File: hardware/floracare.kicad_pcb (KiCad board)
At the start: 2 copper layers, 100 x 100 mm, 17 parts, among them J2 Conn_01x04_Socket, J3 USB_C_Receptacle_USB2.0_16P, J4 Conn_01x04_Socket, J5 Conn_01x14_Socket, J6 Conn_01x05_Socket, U1 AMS1117-3.3, U2 ESP32-S3-WROOM-1

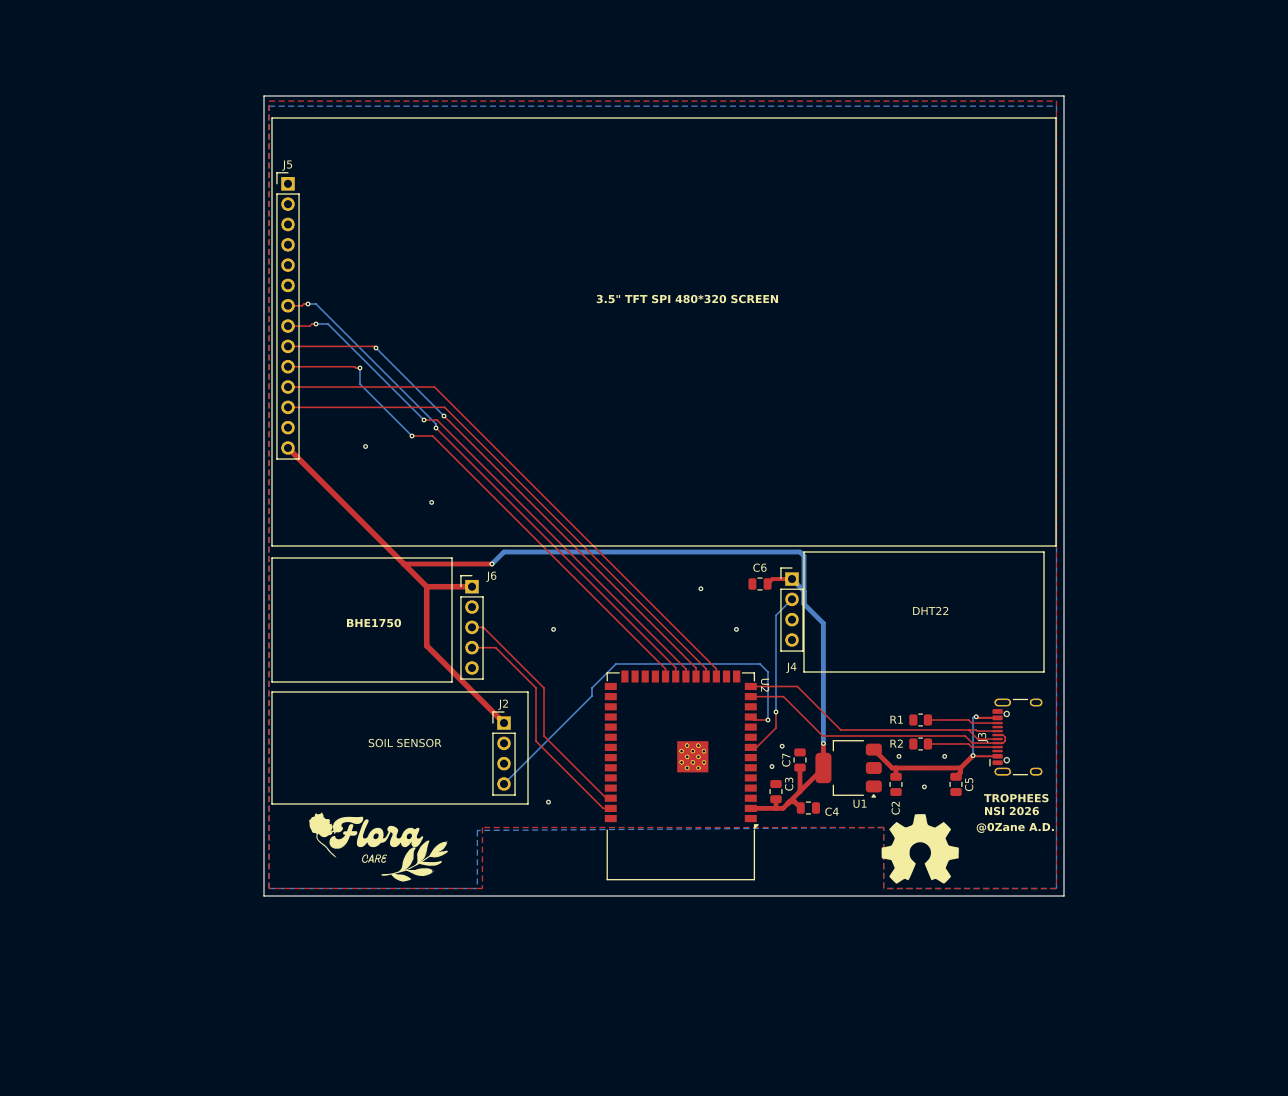
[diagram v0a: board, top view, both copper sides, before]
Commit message: Fixing PCB + adding BOOT and RESET BUTTONS [DRC NOT STABLE]
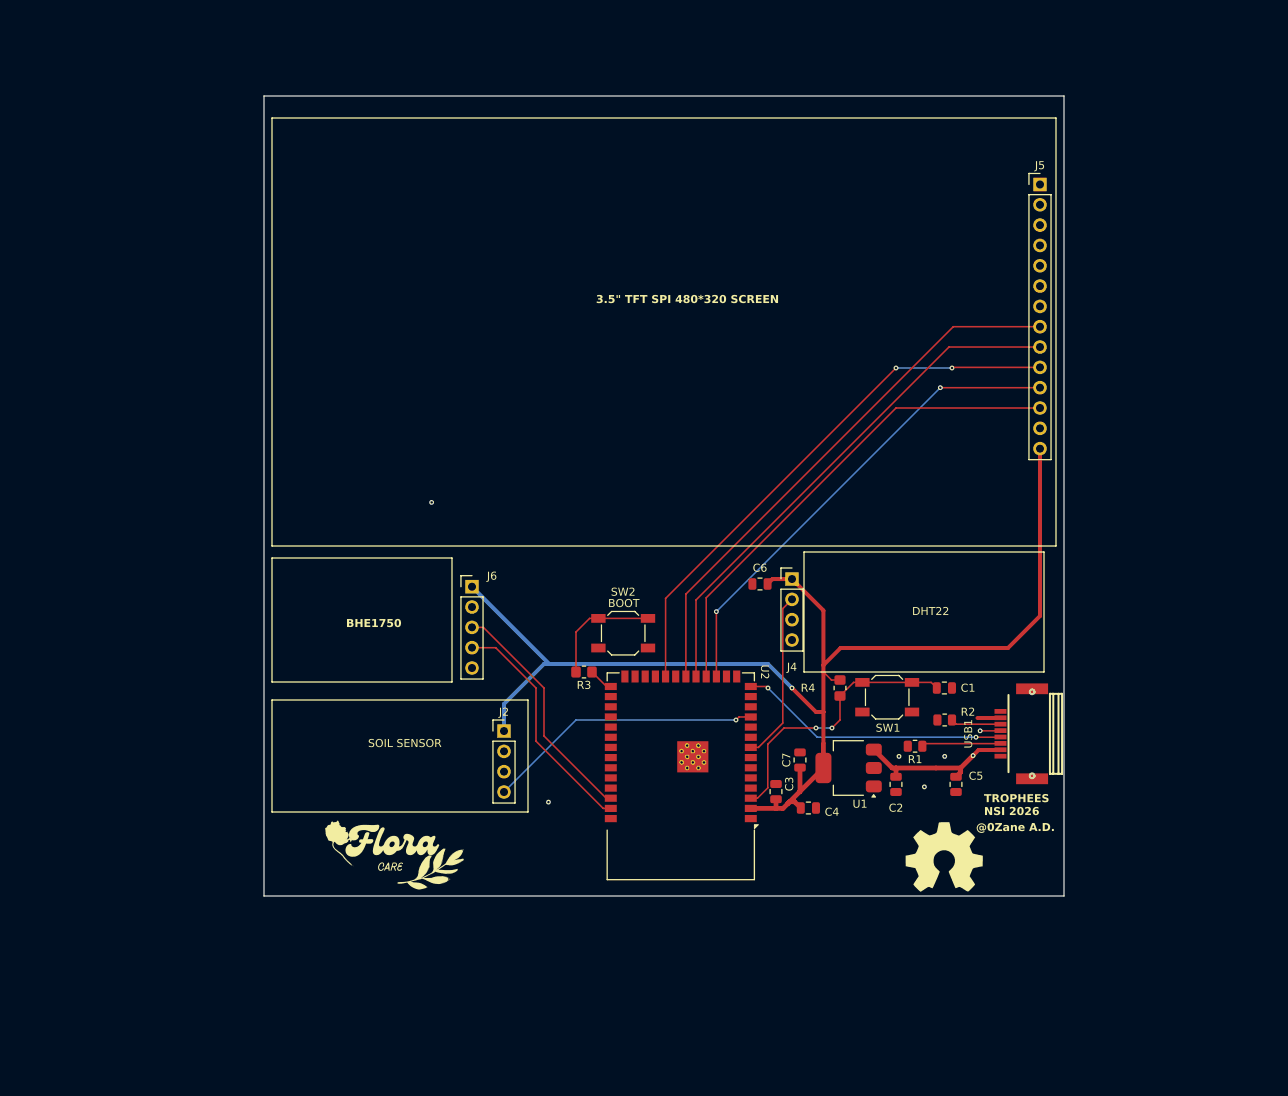
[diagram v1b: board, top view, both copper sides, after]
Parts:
- removed J3: USB_C_Receptacle_USB2.0_16P, Connector_USB:USB_C_Receptacle_HCTL_HC-TYPE-C-16P-01A
- added C1: 0.1uF, Capacitor_SMD:C_0805_2012Metric, F.Cu at (225.5, 99.8)
- added R3: 100, Resistor_SMD:R_0805_2012Metric_Pad1.20x1.40mm_HandSolder, F.Cu at (180.4, 97.8)
- added R4: 5.1K, Resistor_SMD:R_0805_2012Metric_Pad1.20x1.40mm_HandSolder, F.Cu at (212.4, 99.8)
- added SW1: SW_Push, Button_Switch_SMD:SW_SPST_SKQG_WithStem, F.Cu at (218.3, 101.0)
- added SW2: SW_Push, Button_Switch_SMD:SW_SPST_SKQG_WithStem, F.Cu at (185.3, 93.0)
- added USB1: GT-USB-7100A, easyeda2kicad:USB-C-SMD_GT-USB-7100A, F.Cu at (234.5, 105.6)
- moved J5 94.0 mm to (237.4, 36.9)
- moved R2 4.25 mm to (225.5, 103.8)
- moved R1 3.35 mm to (221.8, 107.1)
- moved G*** 3.16 mm to (225.4, 120.8)
- moved G*** 2.24 mm to (156.4, 120.8)
- moved J2 1.00 mm to (170.4, 105.2)
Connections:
- U2 pad 27: unconnected-(U2-IO0-Pad27) -> BOOT
- U2 pad 3: unconnected-(U2-EN-Pad3) -> RESET
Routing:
- net LED: track 68.8 -> 0.00 mm, vias 2 -> 0
- net RESET: track 0.00 -> 34.5 mm, vias 0 -> 2
- net DATA-: track 35.8 -> 2.96 mm, vias 0 -> 1
- net Net-(R3-Pad2): track 0.00 -> 14.7 mm
- net AO_SOIL: track 48.5 -> 35.3 mm
- net RES: track 69.1 -> 60.2 mm, vias 0 -> 2
- net +3V3: track 154.0 -> 160.9 mm, vias 2 -> 1
- net +5V: track 27.4 -> 21.9 mm, vias 2 -> 1
- net CS: track 66.8 -> 61.4 mm
- net DC: track 65.2 -> 68.5 mm
- net BOOT: track 0.00 -> 3.10 mm
- net MOSI: track 68.7 -> 65.7 mm, vias 2 -> 0
- net DATA+: track 37.2 -> 34.3 mm, vias 0 -> 2
- net Net-(USB1-CC2): track 8.87 -> 6.28 mm
- net Net-(USB1-CC1): track 8.87 -> 10.3 mm
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- removed copper zone on B.Cu, net GND
- removed copper zone on F.Cu, net GND
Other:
- board text added: "BOOT"

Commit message: Updating general Project
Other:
- board text added: "RESET"
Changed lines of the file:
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@@
 		(tags "SPST Button Switch")
 		(property "Reference" "SW1"
-			(at 0.1 3.85 0)
+			(at 0.1 -4.15 0)
 			(layer "F.SilkS")
 			(effects
@@
 		)
 		(property "Value" "SW_Push"
-			(at 0.1 -4.15 0)
+			(at 6.1 -4.15 0)
 			(layer "F.Fab")
 			(effects
@@
 		(tags "capacitor")
 		(property "Reference" "C6"
-			(at 0 2 0)
+			(at 0 -2 0)
 			(layer "F.SilkS")
 			(effects
@@
 	)
 	(gr_text "TROPHEES \nNSI 2026\n"
-		(at 230.42 115.85 0)
+		(at 231.42 120.85 0)
 		(layer "F.SilkS")
 		(effects
@@
 	)
 	(gr_text "@0Zane A.D."
-		(at 229.42 117.85 0)
+		(at 230.42 123.85 0)
 		(layer "F.SilkS")
 		(effects
@@
 			)
 			(justify left bottom)
+		)
+	)
+	(gr_text "RESET\n"
+		(at 212.62 105.25 0)
+		(layer "F.SilkS")
+		(effects
+			(font
+				(size 1 1)
+				(thickness 0.1)
+			)
+			(justify left bottom)

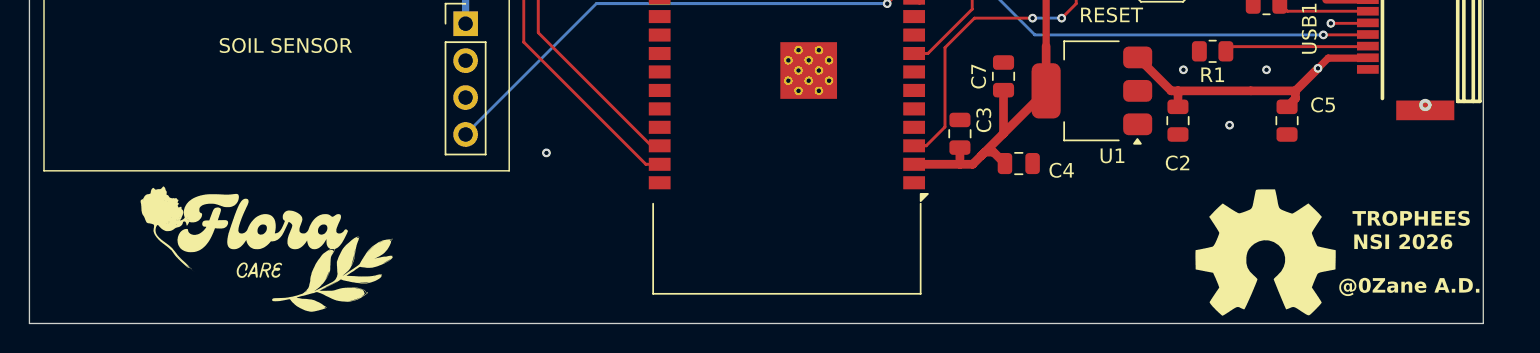
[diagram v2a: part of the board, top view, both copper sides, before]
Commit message: Adding 2 mounting holes
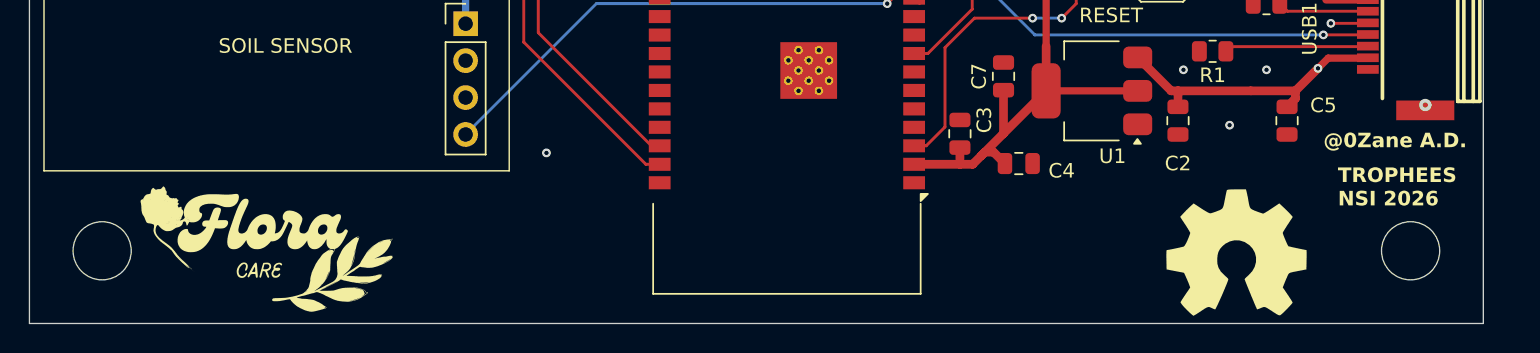
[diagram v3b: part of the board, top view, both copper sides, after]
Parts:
- moved G*** 2.00 mm to (223.4, 120.8)
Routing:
- net +3V3: track 160.9 -> 167.2 mm
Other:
- outline, holes or cut-outs redrawn
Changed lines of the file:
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@@
 	(footprint "LOGO"
 		(layer "F.Cu")
-		(at 225.42 120.85)
+		(at 223.42 120.85)
 		(property "Reference" "G***"
 			(at 0 0 0)
@@
 		(layer "F.SilkS")
 	)
+	(gr_circle
+		(center 145.42 120.85)
+		(end 147.42 120.85)
+		(stroke
+			(width 0.05)
+			(type default)
+		)
+		(fill no)
+		(layer "Edge.Cuts")
+	)
 	(gr_rect
 		(start 140.42 25.85)
@@
 		(layer "Edge.Cuts")
 	)
+	(gr_circle
+		(center 235.42 120.85)
+		(end 237.42 120.85)
+		(stroke
+			(width 0.05)
+			(type default)
+		)
+		(fill no)
+		(layer "Edge.Cuts")
+	)
 	(gr_text "SOIL SENSOR"
 		(at 153.42 107.35 0)
@@
 	)
 	(gr_text "TROPHEES \nNSI 2026\n"
-		(at 231.42 120.85 0)
+		(at 230.42 117.85 0)
 		(layer "F.SilkS")
 		(effects
@@
 	)
 	(gr_text "@0Zane A.D."
-		(at 230.42 123.85 0)
+		(at 229.42 113.85 0)
 		(layer "F.SilkS")
 		(effects
@@
 		)
 	)
+	(dimension
+		(type orthogonal)
+		(layer "Dwgs.User")
+		(pts
+			(xy 240.42 125.85) (xy 235.42 125.85)
+		)
+		(height -5)
+		(orientation 0)
+		(format
+			(prefix "")
+			(suffix "")
+			(units 3)
+			(units_format 0)
+			(precision 4)
+			(suppress_zeroes yes)
+		)
+		(style
+			(thickness 0.1)
+			(arrow_length 1.27)
+			(text_position_mode 0)
+			(arrow_direction outward)
+			(extension_height 0.58642)
+			(extension_offset 0.5)
+			(keep_text_aligned yes)
+		)
+		(gr_text "5"
+			(at 237.92 119.7 0)
+			(layer "Dwgs.User")
+			(effects
+				(font
+					(size 1 1)
+					(thickness 0.15)
+				)
+			)
+		)
+	)
+	(dimension
+		(type orthogonal)
+		(layer "Dwgs.User")
+		(pts
+			(xy 240.42 125.85) (xy 240.42 120.85)
+		)
+		(height 0)
+		(orientation 1)
+		(format
+			(prefix "")
+			(suffix "")
+			(units 3)
+			(units_format 0)
+			(precision 4)
+			(suppress_zeroes yes)
+		)
+		(style
+			(thickness 0.1)
+			(arrow_length 1.27)
+			(text_position_mode 0)
+			(arrow_direction outward)
+			(extension_height 0.58642)
+			(extension_offset 0.5)
+			(keep_text_aligned yes)
+		)
+		(gr_text "5"
+			(at 239.27 123.35 90)
+			(layer "Dwgs.User")
+			(effects
+				(font
+					(size 1 1)
+					(thickness 0.15)
+				)
+			)
+		)
+	)
 	(segment
 		(start 201.27 99.66)
@@
 		(width 0.5)
 		(layer "F.Cu")
+		(net 6)
+	)
+	(segment
+		(start 216.65 109.85)
+		(end 210.35 109.85)
+		(width 0.5)
+		(layer "F.Cu")

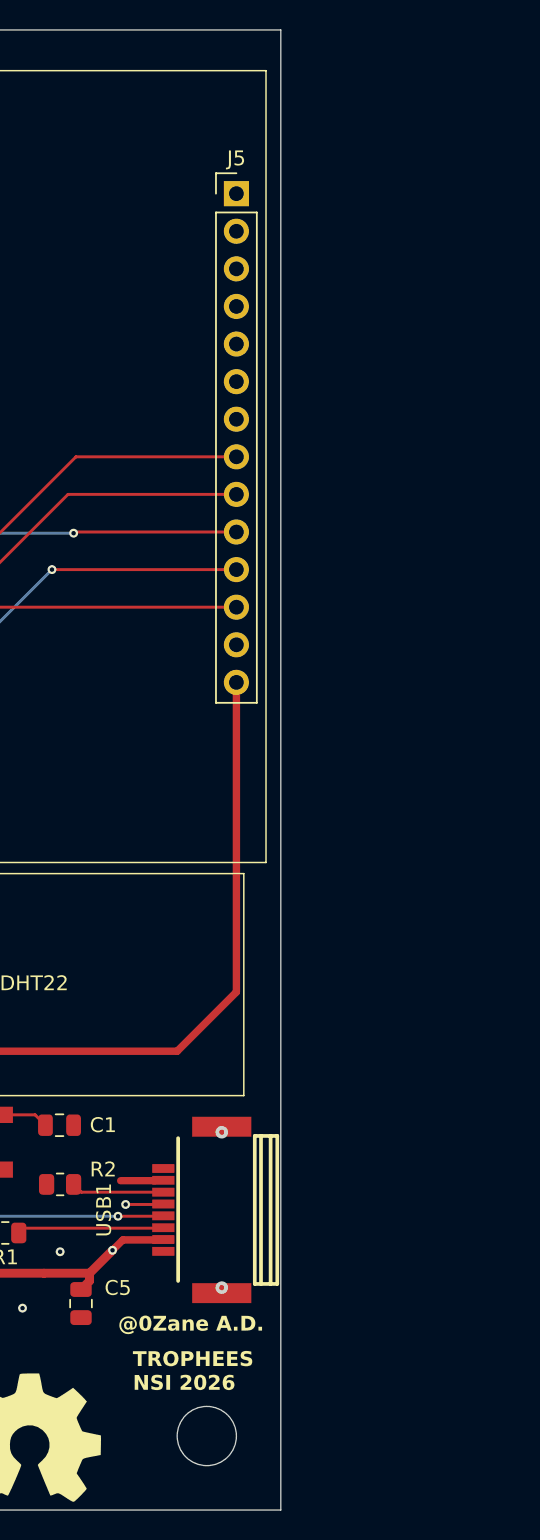
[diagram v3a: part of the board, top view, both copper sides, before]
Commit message: Replacing usb slot
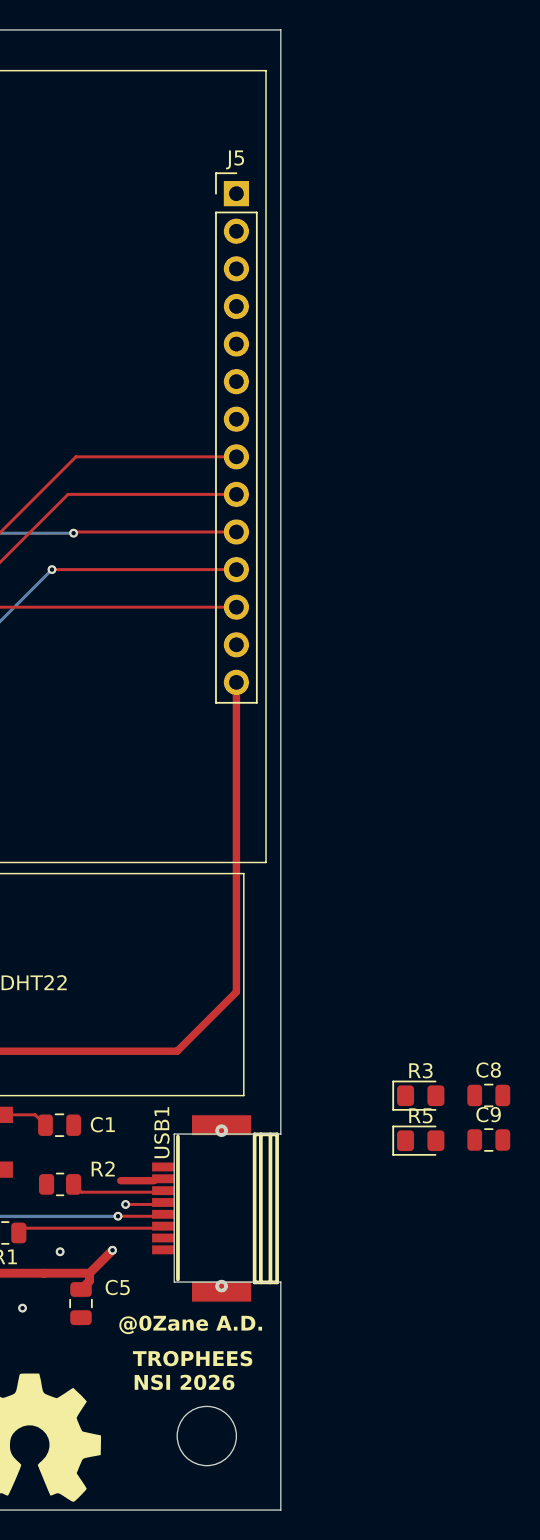
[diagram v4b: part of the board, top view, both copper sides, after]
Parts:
- added C8: 0.1uF, Capacitor_SMD:C_0805_2012Metric, F.Cu at (254.5, 97.8)
- added C9: 0.1uF, Capacitor_SMD:C_0805_2012Metric, F.Cu at (254.5, 100.8)
- added R3: 22, LED_SMD:LED_0805_2012Metric_Pad1.15x1.40mm_HandSolder, F.Cu at (249.9, 97.9)
- added R5: 22, LED_SMD:LED_0805_2012Metric_Pad1.15x1.40mm_HandSolder, F.Cu at (249.9, 100.9)
- R4: value 5.1K -> 10k
- moved USB1 0.10 mm to (234.4, 105.5)
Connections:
- SW2 pad 1: Net-(R3-Pad2) -> BOOT
- SW2 pad 2: GND -> +3V3
- U2 pad 13: DATA- -> Net-(U2-USB_D-)
- U2 pad 14: DATA+ -> Net-(U2-USB_D+)
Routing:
- net Net-(U2-USB_D+): track 0.00 -> 34.3 mm, vias 0 -> 2
- net DATA+: track 34.3 -> 0.00 mm, vias 2 -> 0
- net +5V: track 21.9 -> 18.8 mm
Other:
- outline, holes or cut-outs redrawn
